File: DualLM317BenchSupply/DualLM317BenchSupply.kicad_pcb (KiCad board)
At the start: 2 copper layers, 99.1 x 99.7 mm, 45 parts, among them CON101 BARREL_JACK, CON102 BARREL_JACK, P101 Vout+, P102 Vout-, SW101 SPDT, SW102 SPDT, SW103 SPDT, SW201 DP6T, U101 78L05, U102 LM317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

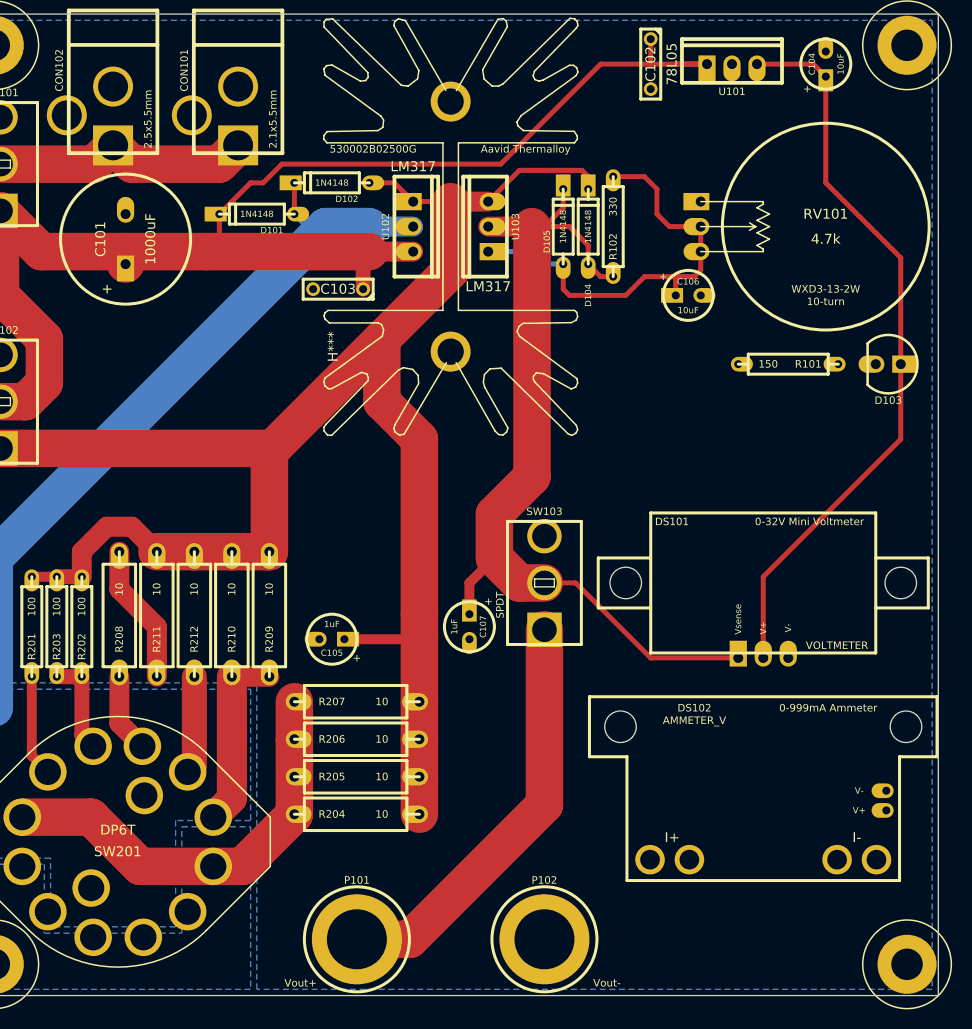
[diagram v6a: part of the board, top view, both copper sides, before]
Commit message: correcting pads for ammeter and running traces to it
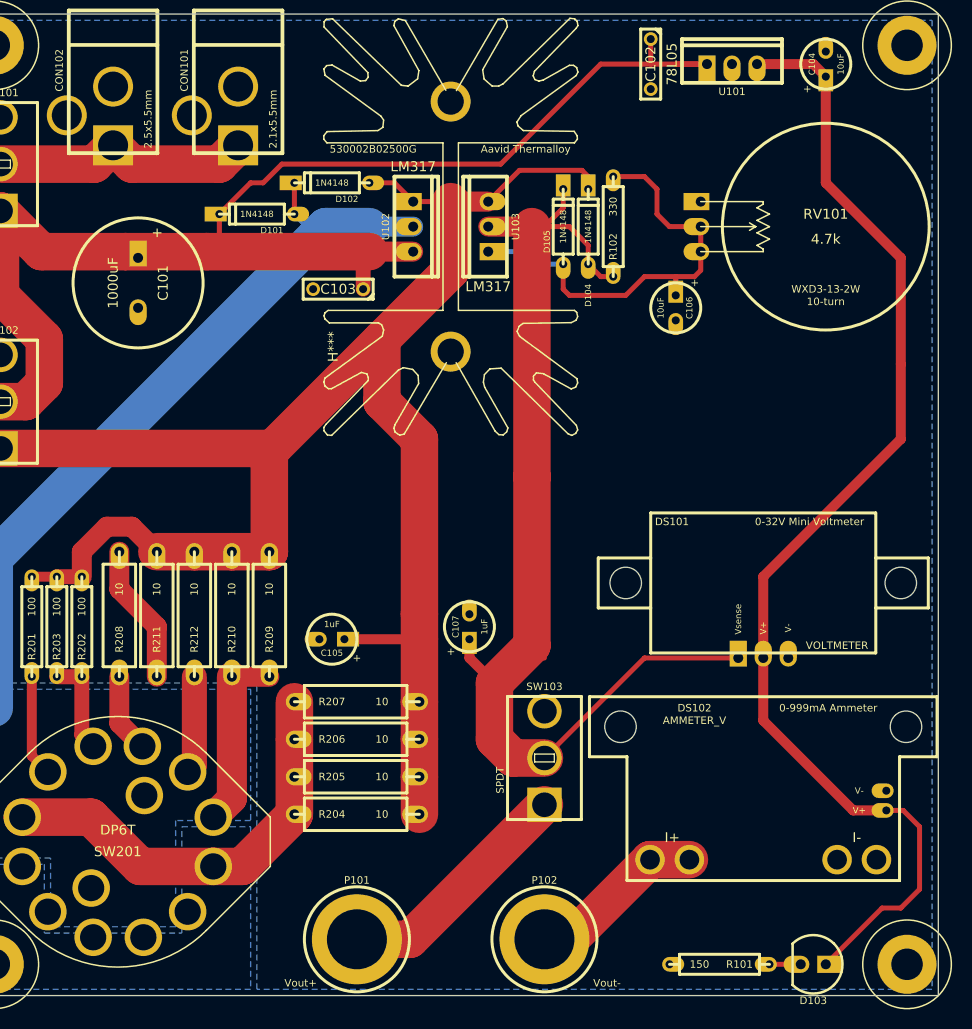
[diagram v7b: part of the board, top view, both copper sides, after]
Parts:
- moved D103 61.4 mm to (224.2, 211.5)
- moved R101 61.4 mm to (218.4, 211.5)
- moved SW103 17.8 mm to (195.6, 190.5)
- moved C107 2.54 mm to (188.0, 178.4), turned to 90 degrees
- moved C101 1.42 mm to (154.3, 139.7), turned to 270 degrees
- turned C106 to 270 degrees
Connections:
- DS102 pad 1: (no net) -> N-0000014
- DS102 pad 2: (no net) -> GND
- DS102 pad 3: (no net) -> 5V
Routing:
- net 5V: track 75.5 -> 121.2 mm
- net N-0000016: track 92.8 -> 112.5 mm
- net N-0000014: track 0.00 -> 18.1 mm
- net N-000004: track 42.5 -> 24.7 mm
- net N-000006: track 0.00 -> 3.18 mm
- net N-000001: track 139.8 -> 138.5 mm

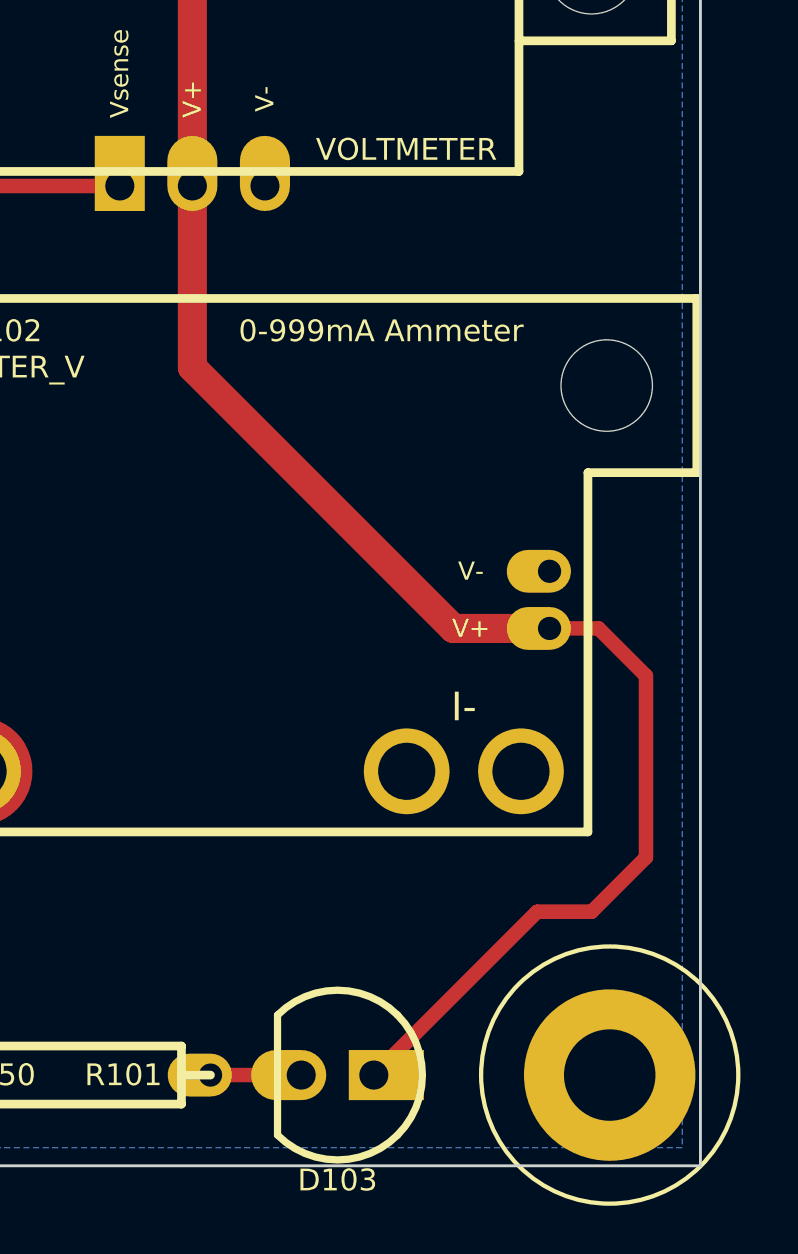
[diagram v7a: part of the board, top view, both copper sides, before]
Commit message: adding caps for meters
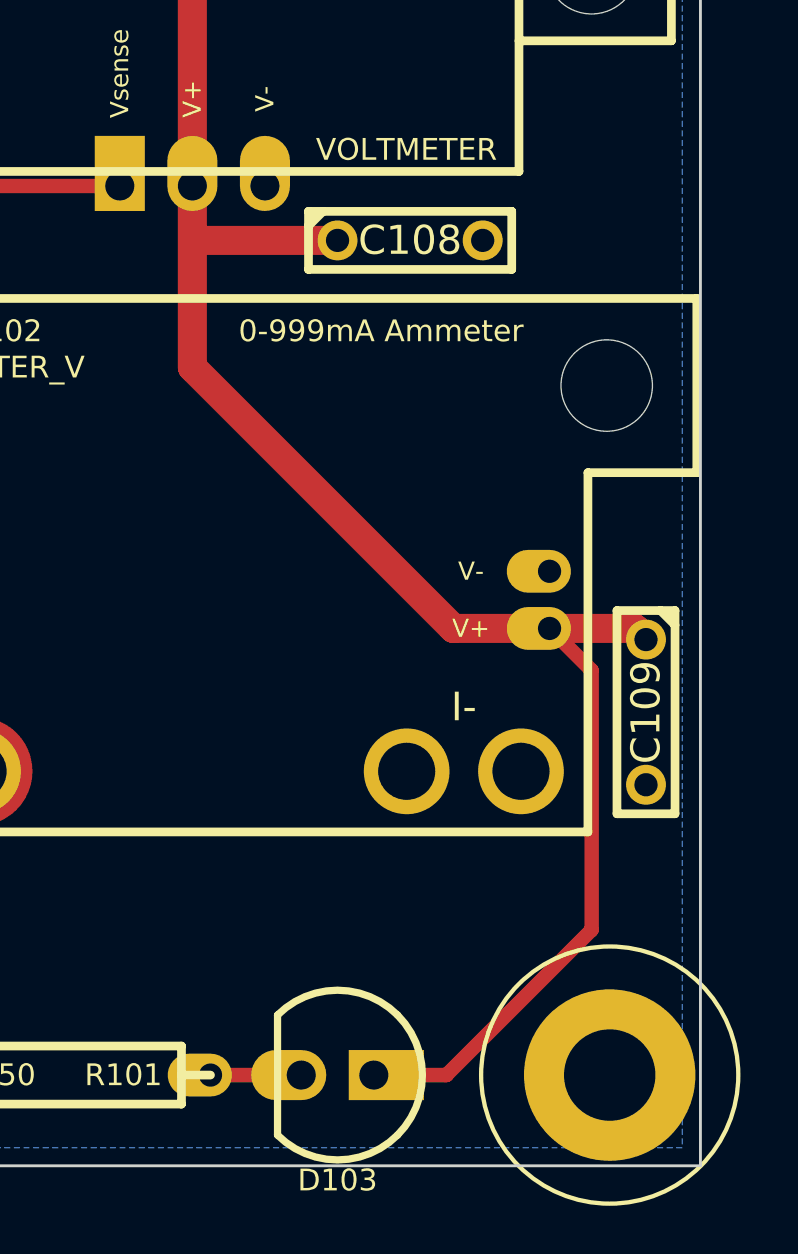
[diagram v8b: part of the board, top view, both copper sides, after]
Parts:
- added C108: 0.1uF, C2, F.Cu at (225.4, 182.2)
- added C109: 0.1uF, C2, F.Cu at (233.7, 198.8)
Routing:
- net 5V: track 121.2 -> 127.6 mm
